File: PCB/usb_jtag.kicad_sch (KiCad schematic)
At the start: 13 parts, among them J4 Pin header, 2x4, J5 Pin header, 2x4, SW1 DSIC01LS-P, U2 CH347F, Y2 8MHz

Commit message: Improve the CH347F schematics and added 3D models
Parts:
- added J6, J7: Pin header, 2x4, Connector_PinHeader_2.54mm:PinHeader_2x04_P2.54mm_Vertical, symbol Connector_Generic:Conn_02x04_Counter_Clockwise
- added R14, R15: 10kΩ, Resistor_SMD:R_0402_1005Metric_Pad0.72x0.64mm_HandSolder, symbol Device:R
- J4, J5: footprint Connector_PinHeader_2.54mm:PinHeader_2x04_P2.54mm_Vertical_SMD -> Connector_PinHeader_2.54mm:PinHeader_2x04_P2.54mm_Vertical; LCSC C22438448 -> C7501275; Part_number IPCP254M08PB28S -> ZX-PZ2.54-2-4PZZ
- renumbered U2 to U3
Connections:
- net CH347.TCK is gone; now on net CH347_TCK: U3.23 (TCK)
- net +3V3: now also R14.1, R15.1
- net GND: now also J6.5 (Pin_5), J6.6 (Pin_6), J6.7 (Pin_7), J6.8 (Pin_8), J7.5 (Pin_5), J7.6 (Pin_6), J7.7 (Pin_7), J7.8 (Pin_8)
- net CH347_SCK: now reaches J4.1 (Pin_1), U3.14 (SCK)
- net CH347_MOSI: now reaches J4.2 (Pin_2), U3.16 (MOSI)
- net CH347_MISO: now reaches J4.3 (Pin_3), U3.15 (MISO)
- net CH347_SCS0: now reaches J4.4 (Pin_4), U3.13 (SCS0)
- net CH347_TCK: now reaches J5.1 (Pin_1)
- net CH347_TCK: no longer U3.4 (TXD1)
- net CH347_RXD1: now reaches U3.5 (RXD1)
- net CH347_RXD1: now also J6.4 (Pin_4); no longer J5.2 (Pin_2)
- net CH347_SCL: now reaches U3.11 (CTS1)
- net CH347_SCL: now also J7.1 (Pin_1), J7.2 (Pin_2), R14.2; no longer J5.3 (Pin_3)
- net CH347_SDA: now reaches U3.12 (RTS1)
- net CH347_SDA: now also J7.3 (Pin_3), J7.4 (Pin_4), R15.2; no longer J5.4 (Pin_4)
- net CH347.TDI renamed CH347_TDI
- net CH347_TDI: now also J5.3 (Pin_3)
- net CH347.TDO renamed CH347_TDO
- net CH347_TDO: now also J5.2 (Pin_2)
- net CH347.TMS renamed CH347_TMS
- net CH347_TMS: now also J5.4 (Pin_4)
- net CH347_RXD renamed CH347_RXD0
- net CH347_RXD0: now also J6.2 (Pin_2)
- net CH347_TXD renamed CH347_TXD0
- net CH347_TXD0: now also J6.1 (Pin_1)
- new net CH347_TXD1: J6.3 (Pin_3), U3.4 (TXD1)
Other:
- moved on the sheet: D1, J4, R13, U3B, U3C, U3E

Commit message: Add LICENSE and minor improvements
- Filled the title blocks
- Connected the LEDs to the FPGA
- Changed the FPGA programming header
- Added USB fuse and capacitors
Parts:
- renumbered C8 to C10, C9 to C11, C10 to C12, C11 to C13, C7 to C9
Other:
- company: (none) -> Copyright (c) 2025 L. Sartory
- title: (none) -> Clavier - 5-in-1 USB
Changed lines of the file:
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@@
 	(generator_version "9.0")
 	(paper "A4")
+	(title_block
+		(title "Clavier - 5-in-1 USB")
+		(date "2025-06-01")
+		(rev "1.0")
+		(company "Copyright (c) 2025 L. Sartory")
+		(comment 1 "SPDX-License-Identifier: CERN-OHL-P-2.0")
+	)
 	(junction
 		(at 73.66 88.9)
@@
 		(on_board yes)
 		(dnp no)
-		(property "Reference" "C10"
+		(property "Reference" "C12"
 			(at 66.421 123.4186 0)
 			(effects
@@
 			(project "clavier"
 				(path "/6362c6e0-59ef-40d3-b6e0-7e9dfe7b9b20/363c396c-f7c0-4911-9972-4574f7737631"
-					(reference "C10")
+					(reference "C12")
 					(unit 1)
 				)
@@
 		(on_board yes)
 		(dnp no)
-		(property "Reference" "C7"
+		(property "Reference" "C9"
 			(at 82.55 68.072 90)
 			(effects
@@
 			(project "clavier"
 				(path "/6362c6e0-59ef-40d3-b6e0-7e9dfe7b9b20/363c396c-f7c0-4911-9972-4574f7737631"
-					(reference "C7")
+					(reference "C9")
 					(unit 1)
 				)
@@
 		(on_board yes)
 		(dnp no)
-		(property "Reference" "C11"
+		(property "Reference" "C13"
 			(at 104.521 123.4186 0)
 			(effects
@@
 			(project "clavier"
 				(path "/6362c6e0-59ef-40d3-b6e0-7e9dfe7b9b20/363c396c-f7c0-4911-9972-4574f7737631"
-					(reference "C11")
+					(reference "C13")
 					(unit 1)
 				)
@@
 		(on_board yes)
 		(dnp no)
-		(property "Reference" "C8"
+		(property "Reference" "C10"
 			(at 66.421 80.2386 0)
 			(effects
@@
 			(project "clavier"
 				(path "/6362c6e0-59ef-40d3-b6e0-7e9dfe7b9b20/363c396c-f7c0-4911-9972-4574f7737631"
-					(reference "C8")
+					(reference "C10")
 					(unit 1)
 				)
@@
 		(on_board yes)
 		(dnp no)
-		(property "Reference" "C9"
+		(property "Reference" "C11"
 			(at 82.55 80.772 90)
 			(effects
@@
 			(project "clavier"
 				(path "/6362c6e0-59ef-40d3-b6e0-7e9dfe7b9b20/363c396c-f7c0-4911-9972-4574f7737631"
-					(reference "C9")
+					(reference "C11")
 					(unit 1)
 				)

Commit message: Place and route peripheral components
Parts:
- removed J4, J5, J6, J7: Pin header, 2x4, Connector_PinHeader_2.54mm:PinHeader_2x04_P2.54mm_Vertical, symbol Connector_Generic:Conn_02x04_Counter_Clockwise
- added J4, J5, J6, J7: Pin header, 2x4, Connector_PinHeader_2.54mm:PinHeader_2x04_P2.54mm_Vertical, symbol Connector_Generic:Conn_02x04_Odd_Even
- renumbered C9 to C12, C10 to C13, C11 to C14, C12 to C15, C13 to C16
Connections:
- net CH347_MISO: now also J4.5 (Pin_5)
- net CH347_MOSI: now also J4.7 (Pin_7)
- net CH347_RXD0: now also J6.3 (Pin_3)
- net CH347_RXD1: now also J6.7 (Pin_7)
- net CH347_SCK: now also J4.3 (Pin_3)
- net CH347_SCL: now also J7.1 (Pin_1), J7.3 (Pin_3)
- net CH347_SCS0: now also J4.1 (Pin_1)
- net CH347_SDA: now also J7.5 (Pin_5), J7.7 (Pin_7)
- net CH347_TCK: now also J5.1 (Pin_1)
- net CH347_TDI: now also J5.5 (Pin_5)
- net CH347_TDO: now also J5.3 (Pin_3)
- net CH347_TMS: now also J5.7 (Pin_7)
- net CH347_TXD0: now also J6.1 (Pin_1)
- net CH347_TXD1: now also J6.5 (Pin_5)
- net GND: now also J4.2 (Pin_2), J4.4 (Pin_4), J4.6 (Pin_6), J4.8 (Pin_8), J5.2 (Pin_2), J5.4 (Pin_4), J5.6 (Pin_6), J5.8 (Pin_8), J6.2 (Pin_2), J6.4 (Pin_4), J6.6 (Pin_6), J6.8 (Pin_8), J7.2 (Pin_2), J7.4 (Pin_4), J7.6 (Pin_6), J7.8 (Pin_8)

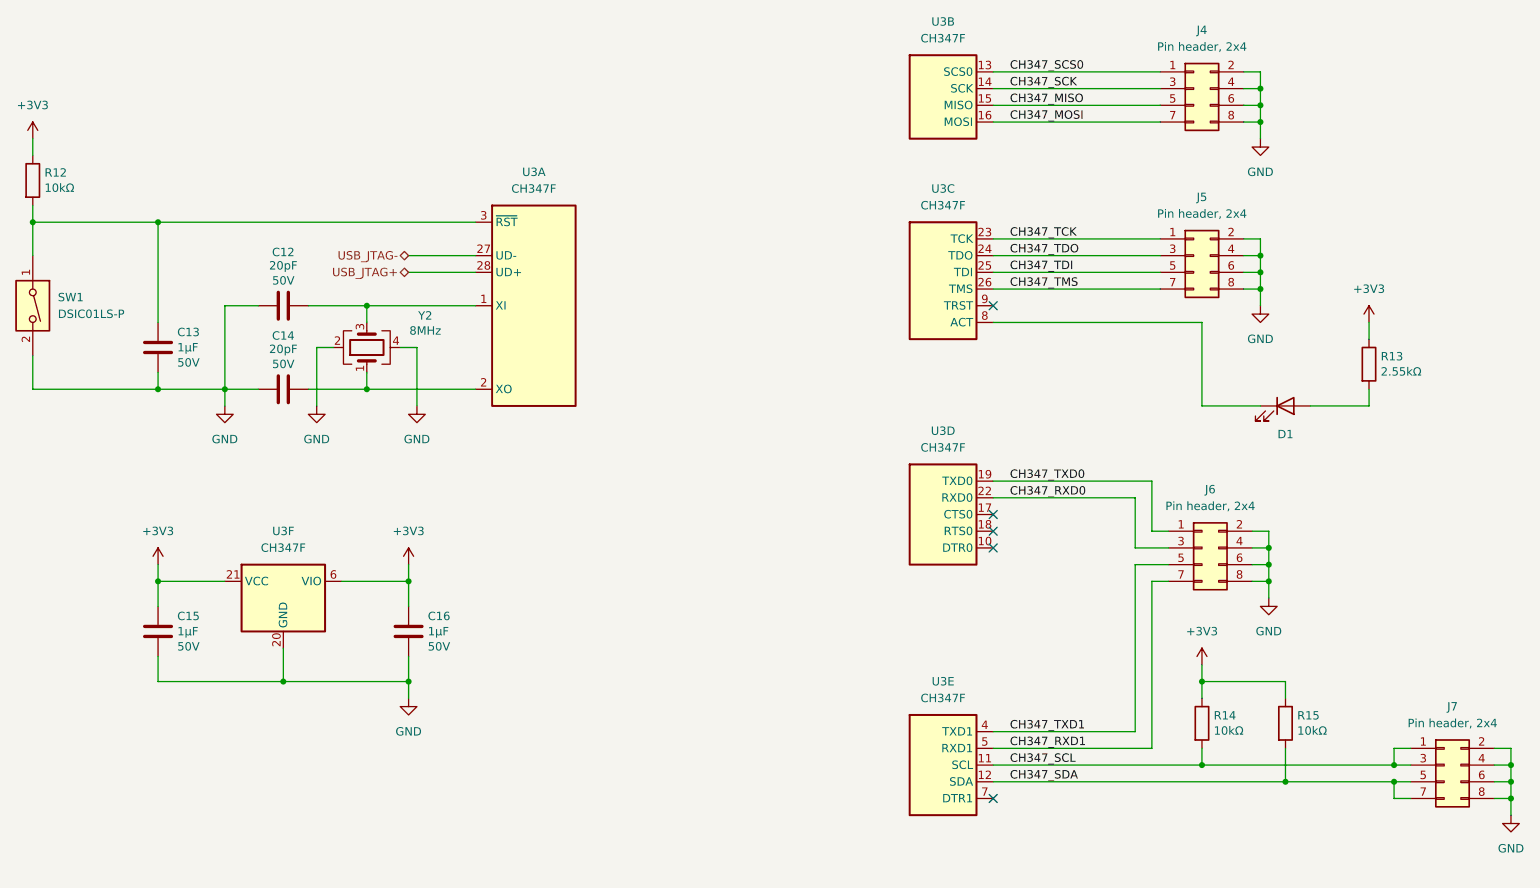
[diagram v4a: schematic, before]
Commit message: Add ESD protection
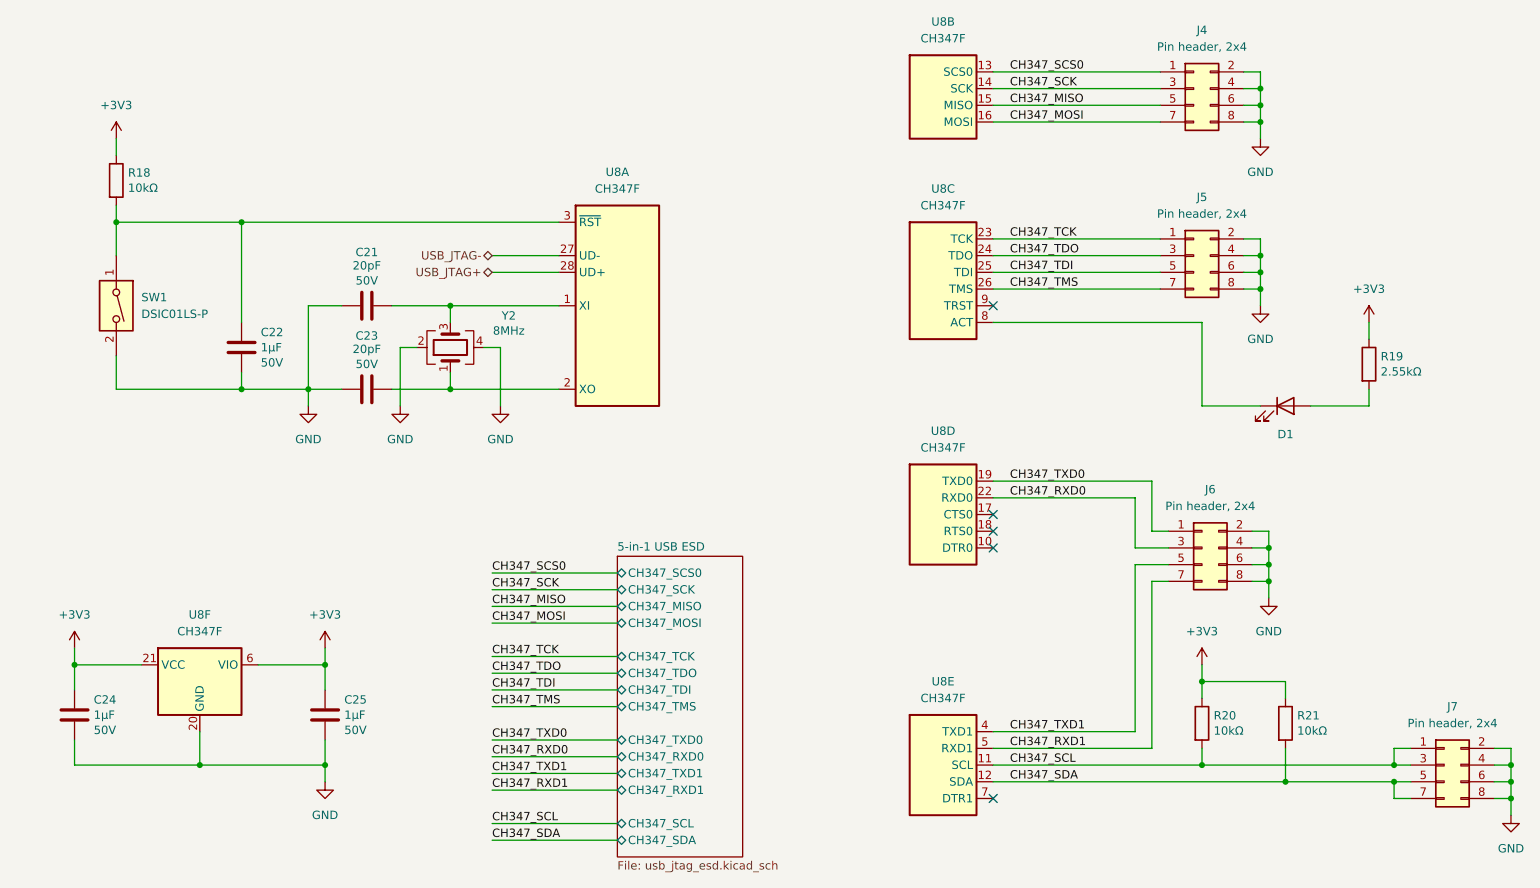
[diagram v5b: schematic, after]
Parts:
- renumbered C12 to C21, C13 to C22, C14 to C23, C15 to C24, C16 to C25, R12 to R18, R13 to R19, R14 to R20, R15 to R21, U3 to U8
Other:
- added sheet 5-in-1 USB ESD (usb_jtag_esd.kicad_sch)
- moved on the sheet: C21, C22, C23, C24, C25, R18, SW1, U8A, U8F, Y2

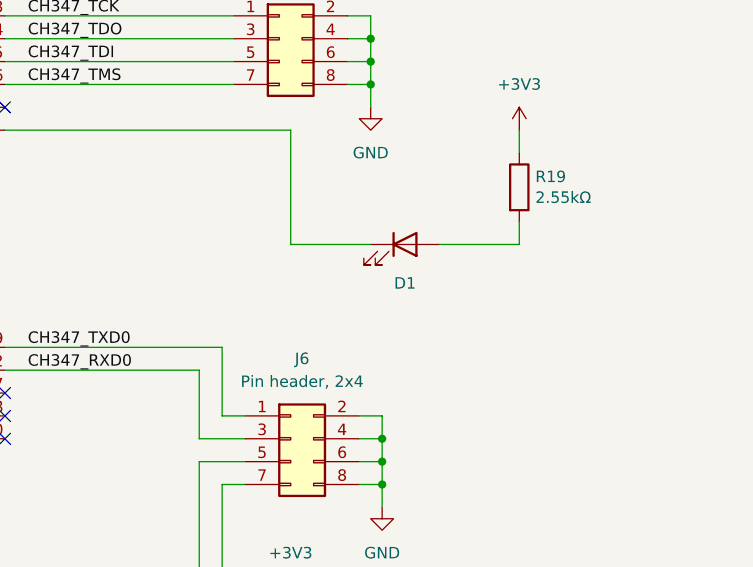
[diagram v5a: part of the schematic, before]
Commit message: Improve the ESD protection
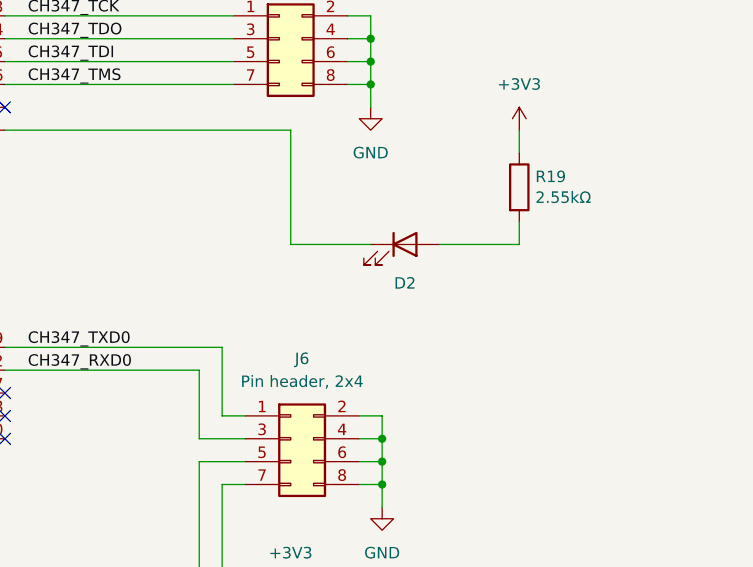
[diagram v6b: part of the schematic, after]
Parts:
- renumbered D1 to D2
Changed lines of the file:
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@@
 		(dnp no)
 		(fields_autoplaced yes)
-		(property "Reference" "#PWR038"
+		(property "Reference" "#PWR040"
 			(at 232.41 127 0)
 			(effects
@@
 			(project "clavier"
 				(path "/6362c6e0-59ef-40d3-b6e0-7e9dfe7b9b20/363c396c-f7c0-4911-9972-4574f7737631"
-					(reference "#PWR038")
+					(reference "#PWR040")
 					(unit 1)
 				)
@@
 		(dnp no)
 		(fields_autoplaced yes)
-		(property "Reference" "#PWR043"
+		(property "Reference" "#PWR045"
 			(at 269.24 160.02 0)
 			(effects
@@
 			(project "clavier"
 				(path "/6362c6e0-59ef-40d3-b6e0-7e9dfe7b9b20/363c396c-f7c0-4911-9972-4574f7737631"
-					(reference "#PWR043")
+					(reference "#PWR045")
 					(unit 1)
 				)
@@
 		(dnp no)
 		(fields_autoplaced yes)
-		(property "Reference" "#PWR032"
+		(property "Reference" "#PWR034"
 			(at 231.14 57.15 0)
 			(effects
@@
 			(project "clavier"
 				(path "/6362c6e0-59ef-40d3-b6e0-7e9dfe7b9b20/363c396c-f7c0-4911-9972-4574f7737631"
-					(reference "#PWR032")
+					(reference "#PWR034")
 					(unit 1)
 				)
@@
 		(dnp no)
 		(fields_autoplaced yes)
-		(property "Reference" "#PWR033"
+		(property "Reference" "#PWR035"
 			(at 231.14 82.55 0)
 			(effects
@@
 			(project "clavier"
 				(path "/6362c6e0-59ef-40d3-b6e0-7e9dfe7b9b20/363c396c-f7c0-4911-9972-4574f7737631"
-					(reference "#PWR033")
+					(reference "#PWR035")
 					(unit 1)
 				)
@@
 		(dnp no)
 		(fields_autoplaced yes)
-		(property "Reference" "#PWR037"
+		(property "Reference" "#PWR039"
 			(at 115.57 97.79 0)
 			(effects
@@
 			(project "clavier"
 				(path "/6362c6e0-59ef-40d3-b6e0-7e9dfe7b9b20/363c396c-f7c0-4911-9972-4574f7737631"
-					(reference "#PWR037")
+					(reference "#PWR039")
 					(unit 1)
 				)
@@
 		(dnp no)
 		(fields_autoplaced yes)
-		(property "Reference" "#PWR034"
+		(property "Reference" "#PWR036"
 			(at 247.65 82.55 0)
 			(effects
@@
 			(project "clavier"
 				(path "/6362c6e0-59ef-40d3-b6e0-7e9dfe7b9b20/363c396c-f7c0-4911-9972-4574f7737631"
-					(reference "#PWR034")
+					(reference "#PWR036")
 					(unit 1)
 				)
@@
 		(dnp no)
 		(fields_autoplaced yes)
-		(property "Reference" "#PWR041"
+		(property "Reference" "#PWR043"
 			(at 222.25 134.62 0)
 			(effects
@@
 			(project "clavier"
 				(path "/6362c6e0-59ef-40d3-b6e0-7e9dfe7b9b20/363c396c-f7c0-4911-9972-4574f7737631"
-					(reference "#PWR041")
+					(reference "#PWR043")
 					(unit 1)
 				)
@@
 		(dnp no)
 		(fields_autoplaced yes)
-		(property "Reference" "#PWR039"
+		(property "Reference" "#PWR041"
 			(at 50.8 132.08 0)
 			(effects
@@
 			(project "clavier"
 				(path "/6362c6e0-59ef-40d3-b6e0-7e9dfe7b9b20/363c396c-f7c0-4911-9972-4574f7737631"
-					(reference "#PWR039")
+					(reference "#PWR041")
 					(unit 1)
 				)
@@
 		(dnp no)
 		(fields_autoplaced yes)
-		(property "Reference" "#PWR036"
+		(property "Reference" "#PWR038"
 			(at 100.33 97.79 0)
 			(effects
@@
 			(project "clavier"
 				(path "/6362c6e0-59ef-40d3-b6e0-7e9dfe7b9b20/363c396c-f7c0-4911-9972-4574f7737631"
-					(reference "#PWR036")
+					(reference "#PWR038")
 					(unit 1)
 				)
@@
 		(dnp no)
 		(fields_autoplaced yes)
-		(property "Reference" "#PWR035"
+		(property "Reference" "#PWR037"
 			(at 86.36 97.79 0)
 			(effects
@@
 			(project "clavier"
 				(path "/6362c6e0-59ef-40d3-b6e0-7e9dfe7b9b20/363c396c-f7c0-4911-9972-4574f7737631"
-					(reference "#PWR035")
+					(reference "#PWR037")
 					(unit 1)
 				)
@@
 		(dnp no)
 		(fields_autoplaced yes)
-		(property "Reference" "#PWR031"
+		(property "Reference" "#PWR033"
 			(at 57.15 54.61 0)
 			(effects
@@
 			(project "clavier"
 				(path "/6362c6e0-59ef-40d3-b6e0-7e9dfe7b9b20/363c396c-f7c0-4911-9972-4574f7737631"
-					(reference "#PWR031")
+					(reference "#PWR033")
 					(unit 1)
 				)
@@
 		(dnp no)
 		(fields_autoplaced yes)
-		(property "Reference" "#PWR042"
+		(property "Reference" "#PWR044"
 			(at 88.9 154.94 0)
 			(effects
@@
 			(project "clavier"
 				(path "/6362c6e0-59ef-40d3-b6e0-7e9dfe7b9b20/363c396c-f7c0-4911-9972-4574f7737631"
-					(reference "#PWR042")
+					(reference "#PWR044")
 					(unit 1)
 				)
@@
 		(on_board yes)
 		(dnp no)
-		(property "Reference" "D1"
+		(property "Reference" "D2"
 			(at 234.95 95.758 0)
 			(effects
@@
 			(project ""
 				(path "/6362c6e0-59ef-40d3-b6e0-7e9dfe7b9b20/363c396c-f7c0-4911-9972-4574f7737631"
-					(reference "D1")
+					(reference "D2")
 					(unit 1)
 				)
@@
 		(dnp no)
 		(fields_autoplaced yes)
-		(property "Reference" "#PWR040"
+		(property "Reference" "#PWR042"
 			(at 88.9 132.08 0)
 			(effects
@@
 			(project "clavier"
 				(path "/6362c6e0-59ef-40d3-b6e0-7e9dfe7b9b20/363c396c-f7c0-4911-9972-4574f7737631"
-					(reference "#PWR040")
+					(reference "#PWR042")
 					(unit 1)
 				)
